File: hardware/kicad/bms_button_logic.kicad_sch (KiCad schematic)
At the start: 15 parts, among them Q18 L2N7002SLLT1G, SW2 TC-6615-5-260G, U82 NCP718ASN330T1G, U84 PMEG10030ELPX

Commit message: starting erc check
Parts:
- C130, C132, C134: footprint Capacitor_SMD:C_0603_1608Metric -> 5v rail sm-easyedapro:C0603
- F5: footprint Fuse:Fuse_1206_3216Metric -> 5v rail sm-easyedapro:F1206
- Q18: footprint Package_TO_SOT_SMD:SOT-23 -> 5v rail sm-easyedapro:SOT-23-3_L3.0-W1.7-P0.95-LS2.9-BR
- R213, R214, R215, R216: footprint Resistor_SMD:R_0603_1608Metric -> 5v rail sm-easyedapro:R0603
- U82: footprint Package_TO_SOT_SMD:TSOT-23-5 -> 5v rail sm-easyedapro:TSOT-23-5_L2.9-W1.6-P0.95-LS2.8-BL
- U84: footprint Diode_SMD:SOD-128 -> 5v rail sm-easyedapro:SOD-128_L3.7-W2.5-LS4.7-RD
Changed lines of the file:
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@@
 			)
 		)
-		(property "Footprint" "Resistor_SMD:R_0603_1608Metric"
+		(property "Footprint" "5v rail sm-easyedapro:R0603"
 			(at 158.75 124.46 0)
 			(effects
@@
 			)
 		)
-		(property "Footprint" "Resistor_SMD:R_0603_1608Metric"
+		(property "Footprint" "5v rail sm-easyedapro:R0603"
 			(at 207.01 124.46 0)
 			(effects
@@
 			)
 		)
-		(property "Footprint" "Capacitor_SMD:C_0603_1608Metric"
+		(property "Footprint" "5v rail sm-easyedapro:C0603"
 			(at 60.96 96.52 0)
 			(effects
@@
 			)
 		)
-		(property "Footprint" "Package_TO_SOT_SMD:TSOT-23-5"
+		(property "Footprint" "5v rail sm-easyedapro:TSOT-23-5_L2.9-W1.6-P0.95-LS2.8-BL"
 			(at 90.17 81.28 0)
 			(effects
@@
 			)
 		)
-		(property "Footprint" "Resistor_SMD:R_0603_1608Metric"
+		(property "Footprint" "5v rail sm-easyedapro:R0603"
 			(at 76.2 97.79 0)
 			(effects
@@
 			)
 		)
-		(property "Footprint" "Capacitor_SMD:C_0603_1608Metric"
+		(property "Footprint" "5v rail sm-easyedapro:C0603"
 			(at 186.69 124.46 0)
 			(effects
@@
 			)
 		)
-		(property "Footprint" "Fuse:Fuse_1206_3216Metric"
+		(property "Footprint" "5v rail sm-easyedapro:F1206"
 			(at 49.53 78.74 0)
 			(effects
@@
 			)
 		)
-		(property "Footprint" "Diode_SMD:SOD-128"
+		(property "Footprint" "5v rail sm-easyedapro:SOD-128_L3.7-W2.5-LS4.7-RD"
 			(at 147.32 80.01 0)
 			(effects
@@
 			)
 		)
-		(property "Footprint" "Resistor_SMD:R_0603_1608Metric"
+		(property "Footprint" "5v rail sm-easyedapro:R0603"
 			(at 207.01 68.58 0)
 			(effects
@@
 			)
 		)
-		(property "Footprint" "Capacitor_SMD:C_0603_1608Metric"
+		(property "Footprint" "5v rail sm-easyedapro:C0603"
 			(at 105.41 93.98 0)
 			(effects
@@
 			)
 		)
-		(property "Footprint" "Package_TO_SOT_SMD:SOT-23"
+		(property "Footprint" "5v rail sm-easyedapro:SOT-23-3_L3.0-W1.7-P0.95-LS2.9-BR"
 			(at 186.69 95.25 0)
 			(effects

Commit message: various updates
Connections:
- net GND: now reaches SW2.3
- net GND: now also SW2.4
- no-connect marks 3 -> 1
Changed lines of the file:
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@@
 		(at 101.6 82.55)
-	)
-	(no_connect
-		(at 204.47 100.33)
-	)
-	(no_connect
-		(at 204.47 90.17)
 	)
 	(wire
@@
 			)
 			(justify left)
+		)
+	)
+	(symbol
+		(lib_id "power:GND")
+		(at 204.47 100.33 0)
+		(unit 1)
+		(exclude_from_sim no)
+		(in_bom yes)
+		(on_board yes)
+		(dnp no)
+		(fields_autoplaced yes)
+		(property "Reference" "#PWR04501"
+			(at 204.47 106.68 0)
+			(effects
+				(font
+					(size 1.27 1.27)
+				)
+				(hide yes)
+			)
+		)
+		(property "Value" "GND"
+			(at 204.47 105.41 0)
+			(effects
+				(font
+					(size 1.27 1.27)
+				)
+			)
+		)
+		(property "Footprint" ""
+			(at 204.47 100.33 0)
+			(effects
+				(font
+					(size 1.27 1.27)
+				)
+				(hide yes)
+			)
+		)
+		(property "Datasheet" ""
+			(at 204.47 100.33 0)
+			(effects
+				(font
+					(size 1.27 1.27)
+				)
+				(hide yes)
+			)
+		)
+		(property "Description" "Power symbol creates a global label with name \"GND\" , ground"
+			(at 204.47 100.33 0)
+			(effects
+				(font
+					(size 1.27 1.27)
+				)
+				(hide yes)
+			)
+		)
+		(pin "1"
+		)
+		(instances
+			(project ""
+				(path "/3f85abf4-0b95-4c4a-b7e9-06f59ca1ea3d/5c2e021f-c2d4-49e2-8c36-9a64f1f12001/261b4c59-ebc7-47a2-bb10-0e71ece0f9bf"
+					(reference "#PWR04501")
+					(unit 1)
+				)
+			)
 		)
 	)
@@
 					(unit 1)
 				)
+			)
+		)
+	)
+	(symbol
+		(lib_id "power:GND")
+		(at 204.47 90.17 180)
+		(unit 1)
+		(exclude_from_sim no)
+		(in_bom yes)
+		(on_board yes)
+		(dnp no)
+		(fields_autoplaced yes)
+		(property "Reference" "#PWR04502"
+			(at 204.47 83.82 0)
+			(effects
+				(font
+					(size 1.27 1.27)
+				)
+				(hide yes)
+			)
+		)
+		(property "Value" "GND"
+			(at 204.47 85.09 0)
+			(effects
+				(font
+					(size 1.27 1.27)
+				)
+			)
+		)
+		(property "Footprint" ""
+			(at 204.47 90.17 0)
+			(effects
+				(font
+					(size 1.27 1.27)
+				)
+				(hide yes)
+			)
+		)
+		(property "Datasheet" ""
+			(at 204.47 90.17 0)
+			(effects
+				(font
+					(size 1.27 1.27)
+				)
+				(hide yes)
+			)
+		)
+		(property "Description" "Power symbol creates a global label with name \"GND\" , ground"
+			(at 204.47 90.17 0)
+			(effects
+				(font
+					(size 1.27 1.27)
+				)
+				(hide yes)
+			)
+		)
+		(pin "1"
+		)
+		(instances
+			(project "svea_powerboard_rev3"
+				(path "/3f85abf4-0b95-4c4a-b7e9-06f59ca1ea3d/5c2e021f-c2d4-49e2-8c36-9a64f1f12001/261b4c59-ebc7-47a2-bb10-0e71ece0f9bf"
+					(reference "#PWR04502")
+					(unit 1)
+				)

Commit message: updates
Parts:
- removed SW2: TC-6615-5-260G, JLCImport:TC-6615-5-260G, symbol JLCImport:TC-6615-5-260G
- added BMS_Bypass_5V_SW3601: ~, 5v rail sm-easyedapro:SW-SMD_L3.9-W3.0-P4.45, symbol 5v rail sm-easyedapro:TS-1088-AR02016
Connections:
- net Button/HIGH: now also BMS_Bypass_5V_SW3601.2
- net Button/LOW: now also BMS_Bypass_5V_SW3601.1

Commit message: updating symbols to use kicad footprints where possible
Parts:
- C130, C132, C134: footprint 5v rail sm-easyedapro:C0603 -> Capacitor_SMD:C_0603_1608Metric
- R213, R214, R215, R216: footprint 5v rail sm-easyedapro:R0603 -> Resistor_SMD:R_0603_1608Metric
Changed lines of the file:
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@@
 			)
 		)
-		(property "Footprint" "5v rail sm-easyedapro:R0603"
+		(property "Footprint" "Resistor_SMD:R_0603_1608Metric"
 			(at 158.75 124.46 0)
 			(effects
@@
 			)
 		)
-		(property "Footprint" "5v rail sm-easyedapro:R0603"
+		(property "Footprint" "Resistor_SMD:R_0603_1608Metric"
 			(at 207.01 124.46 0)
 			(effects
@@
 			)
 		)
-		(property "Footprint" "5v rail sm-easyedapro:C0603"
+		(property "Footprint" "Capacitor_SMD:C_0603_1608Metric"
 			(at 60.96 96.52 0)
 			(effects
@@
 			)
 		)
-		(property "Footprint" "5v rail sm-easyedapro:R0603"
+		(property "Footprint" "Resistor_SMD:R_0603_1608Metric"
 			(at 76.2 97.79 0)
 			(effects
@@
 			)
 		)
-		(property "Footprint" "5v rail sm-easyedapro:C0603"
+		(property "Footprint" "Capacitor_SMD:C_0603_1608Metric"
 			(at 186.69 124.46 0)
 			(effects
@@
 			)
 		)
-		(property "Footprint" "5v rail sm-easyedapro:R0603"
+		(property "Footprint" "Resistor_SMD:R_0603_1608Metric"
 			(at 207.01 68.58 0)
 			(effects
@@
 			)
 		)
-		(property "Footprint" "5v rail sm-easyedapro:C0603"
+		(property "Footprint" "Capacitor_SMD:C_0603_1608Metric"
 			(at 105.41 93.98 0)
 			(effects

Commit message: switched some more
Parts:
- F5: footprint 5v rail sm-easyedapro:F1206 -> Fuse:Fuse_1206_3216Metric
- Q18: footprint 5v rail sm-easyedapro:SOT-23-3_L3.0-W1.7-P0.95-LS2.9-BR -> Package_TO_SOT_SMD:SOT-23
- U82: footprint 5v rail sm-easyedapro:TSOT-23-5_L2.9-W1.6-P0.95-LS2.8-BL -> Package_TO_SOT_SMD:TSOT-23-5
- U84: footprint 5v rail sm-easyedapro:SOD-128_L3.7-W2.5-LS4.7-RD -> Diode_SMD:SOD-128
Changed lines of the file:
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@@
 			)
 		)
-		(property "Footprint" "5v rail sm-easyedapro:TSOT-23-5_L2.9-W1.6-P0.95-LS2.8-BL"
+		(property "Footprint" "Package_TO_SOT_SMD:TSOT-23-5"
 			(at 90.17 81.28 0)
 			(effects
@@
 			)
 		)
-		(property "Footprint" "5v rail sm-easyedapro:F1206"
+		(property "Footprint" "Fuse:Fuse_1206_3216Metric"
 			(at 49.53 78.74 0)
 			(effects
@@
 			)
 		)
-		(property "Footprint" "5v rail sm-easyedapro:SOD-128_L3.7-W2.5-LS4.7-RD"
+		(property "Footprint" "Diode_SMD:SOD-128"
 			(at 147.32 80.01 0)
 			(effects
@@
 			)
 		)
-		(property "Footprint" "5v rail sm-easyedapro:SOT-23-3_L3.0-W1.7-P0.95-LS2.9-BR"
+		(property "Footprint" "Package_TO_SOT_SMD:SOT-23"
 			(at 186.69 95.25 0)
 			(effects

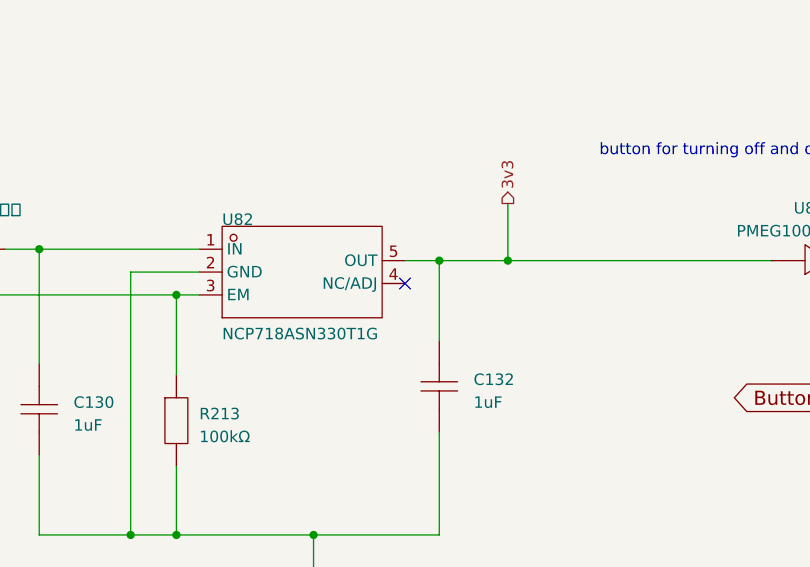
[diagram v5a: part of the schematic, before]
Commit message: starting erc check
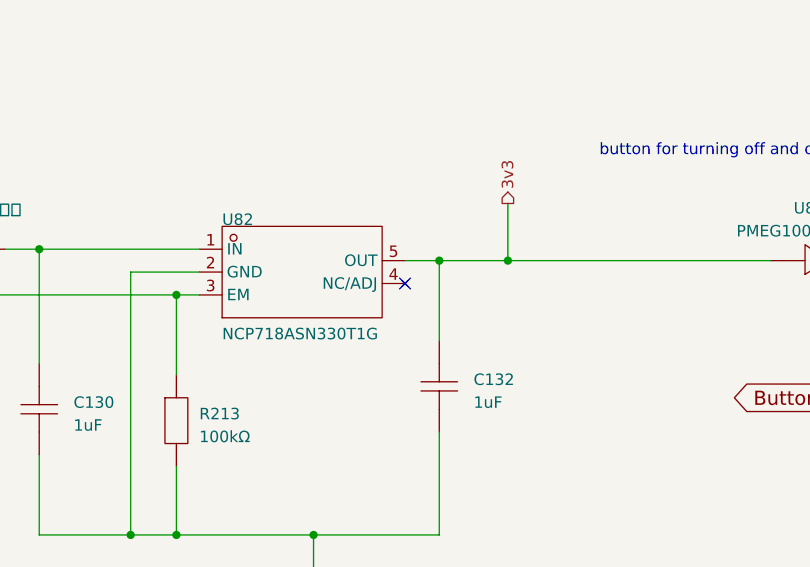
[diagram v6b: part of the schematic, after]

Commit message: various updates
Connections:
- net Button/DIGITAL renamed Button/DIGITAL
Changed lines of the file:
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@@
 		)
 	)
-	(global_label "Button/DIGITAL"
-		(shape output)
+	(global_label "Button{slash}DIGITAL"
+		(shape input)
 		(at 157.48 95.25 180)
 		(effects

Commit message: various erc fixes
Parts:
- U84: footprint Diode_SMD:SOD-128 -> Diode_SMD:D_SOD-128
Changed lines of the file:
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@@
 			)
 		)
-		(property "Footprint" "Diode_SMD:SOD-128"
+		(property "Footprint" "Diode_SMD:D_SOD-128"
 			(at 147.32 80.01 0)
 			(effects
